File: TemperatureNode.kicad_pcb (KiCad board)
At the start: 2 copper layers, 60 x 30 mm, 20 parts, among them J1 Conn_01x02_Pin, U1 ATtiny414-SS, U2 SHT40-AD1B-R3

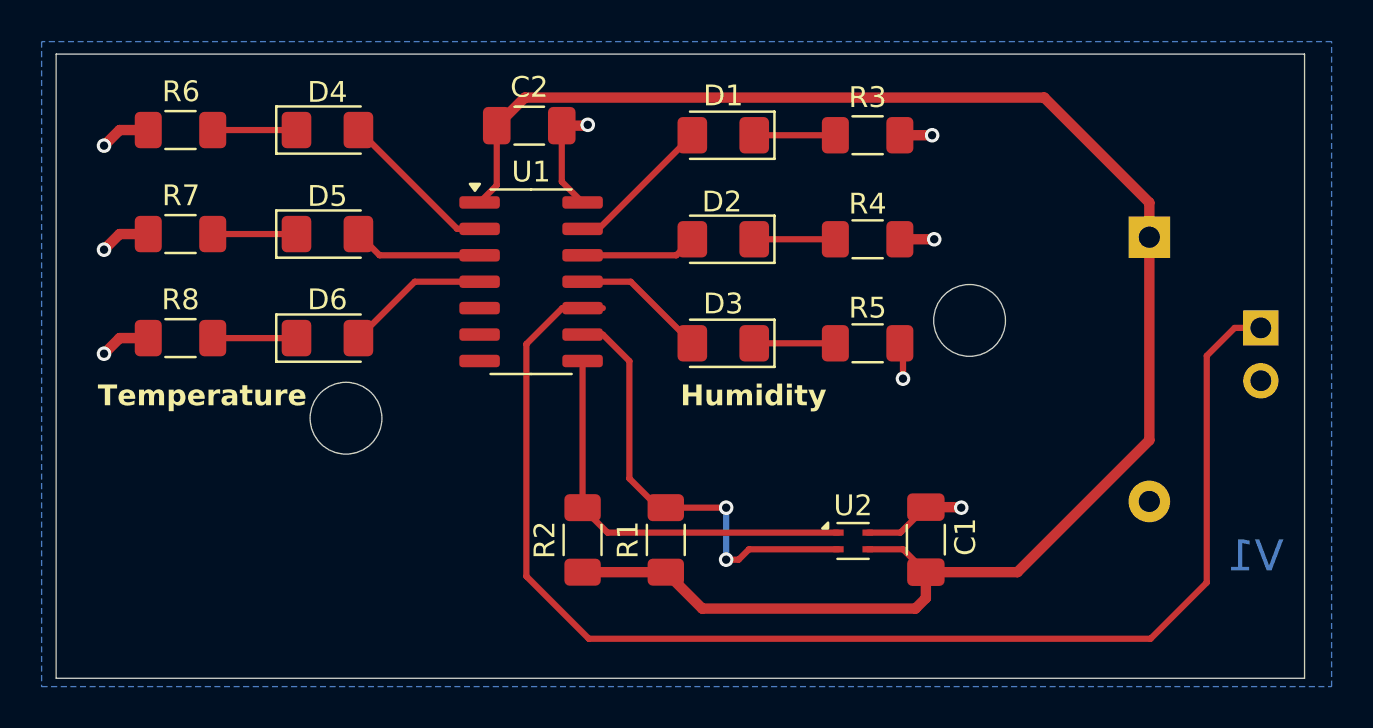
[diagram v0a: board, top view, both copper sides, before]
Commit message: Changed I2C routing to match length and eliminate via
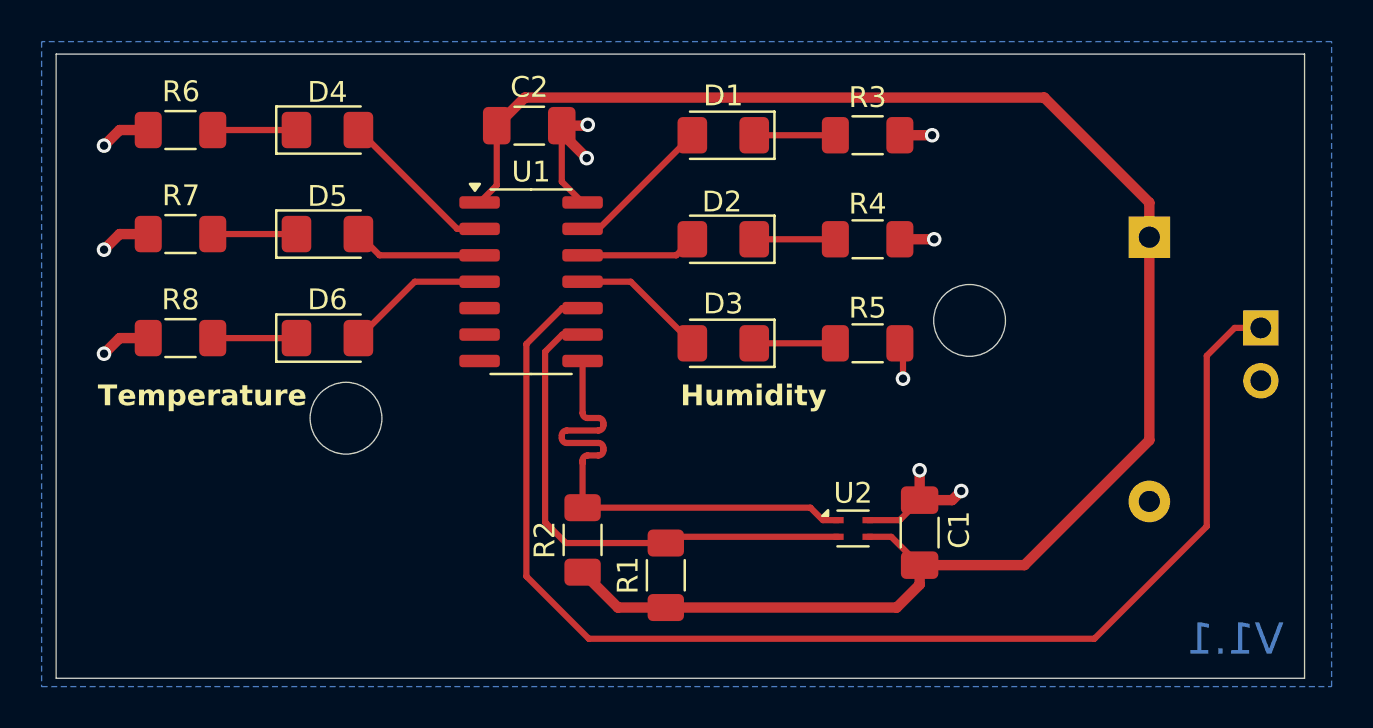
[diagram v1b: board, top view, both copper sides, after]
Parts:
- moved R1 1.70 mm to (164.0, 80.7)
- moved U2 0.60 mm to (173.0, 78.4)
- moved C1 0.45 mm to (176.2, 78.6)
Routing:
- net Net-(U1-PB1): track 19.8 -> 24.7 mm
- net Net-(U1-PB0): track 21.8 -> 25.0 mm, vias 2 -> 0
- net GND: track 22.7 -> 25.6 mm, vias 8 -> 10
- net /UPDI: track 64.7 -> 62.1 mm
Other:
- board text added: "V1.1"
- board text removed: "V1"

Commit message: Added calculations file and updated I2C routing for more clearance
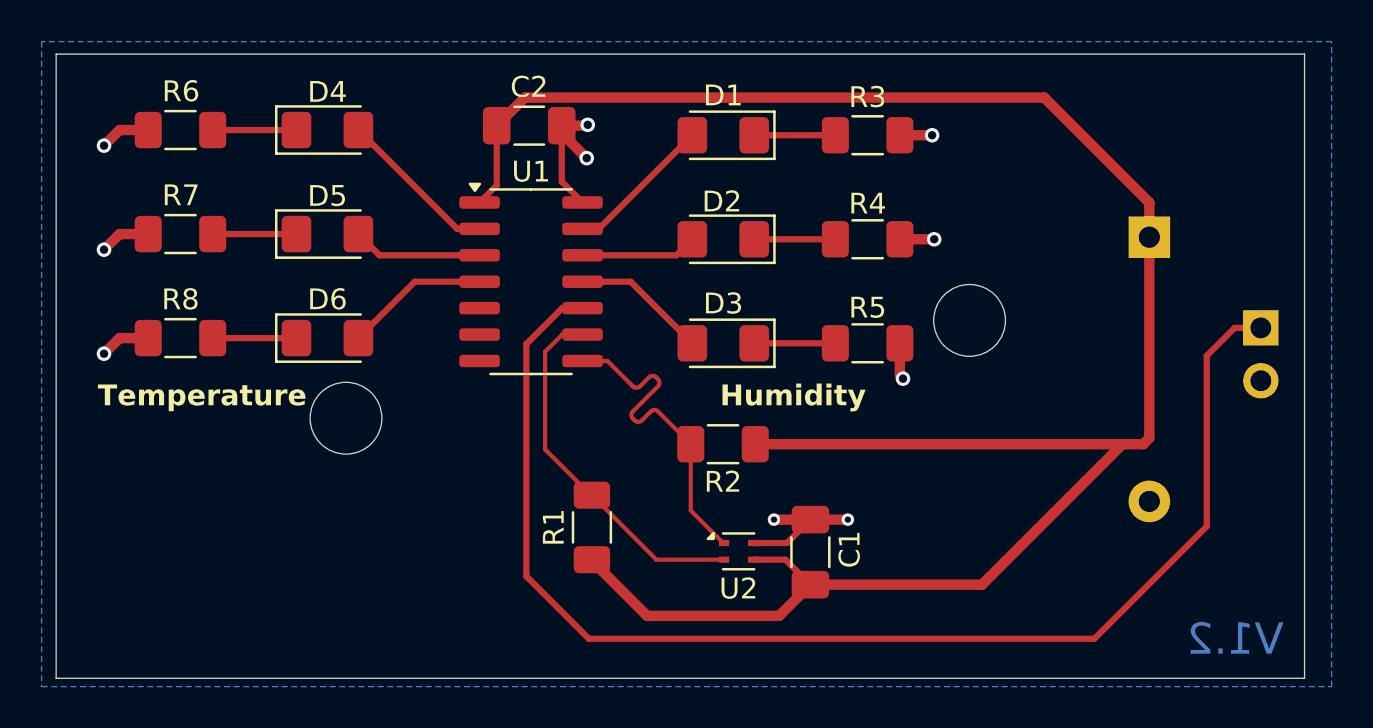
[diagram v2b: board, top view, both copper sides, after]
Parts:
- moved R2 8.17 mm to (166.8, 74.3), turned to 180 degrees
- moved U2 5.61 mm to (167.5, 79.5)
- moved C1 5.33 mm to (170.9, 79.5)
- moved R1 4.23 mm to (160.4, 78.3)
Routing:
- net +3.3V: track 84.4 -> 101.7 mm
- net Net-(U1-PB1): track 24.7 -> 16.0 mm
- net Net-(U1-PB0): track 25.0 -> 17.6 mm
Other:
- board text added: "V1.2"
- board text removed: "V1.1"
